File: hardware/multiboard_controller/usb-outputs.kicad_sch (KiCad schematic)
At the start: 24 parts, among them J2 USB_C_Receptacle, J3 USB_C_Receptacle, J4 USB_C_Receptacle, J5 USB_C_Receptacle, J6 USB_C_Receptacle, J7 USB_C_Receptacle, J8 USB_C_Receptacle, J9 USB_C_Receptacle

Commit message: Adding final connectors and general cleanup.
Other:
- note added: "Nopo all but 2 for validation"
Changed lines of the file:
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@@
+		)
+	)
+	(text "Nopo all but 2 for validation\n"
+		(exclude_from_sim no)
+		(at 138.938 24.384 0)
+		(effects
+			(font
+				(size 1.27 1.27)
+			)
 		)
 	)

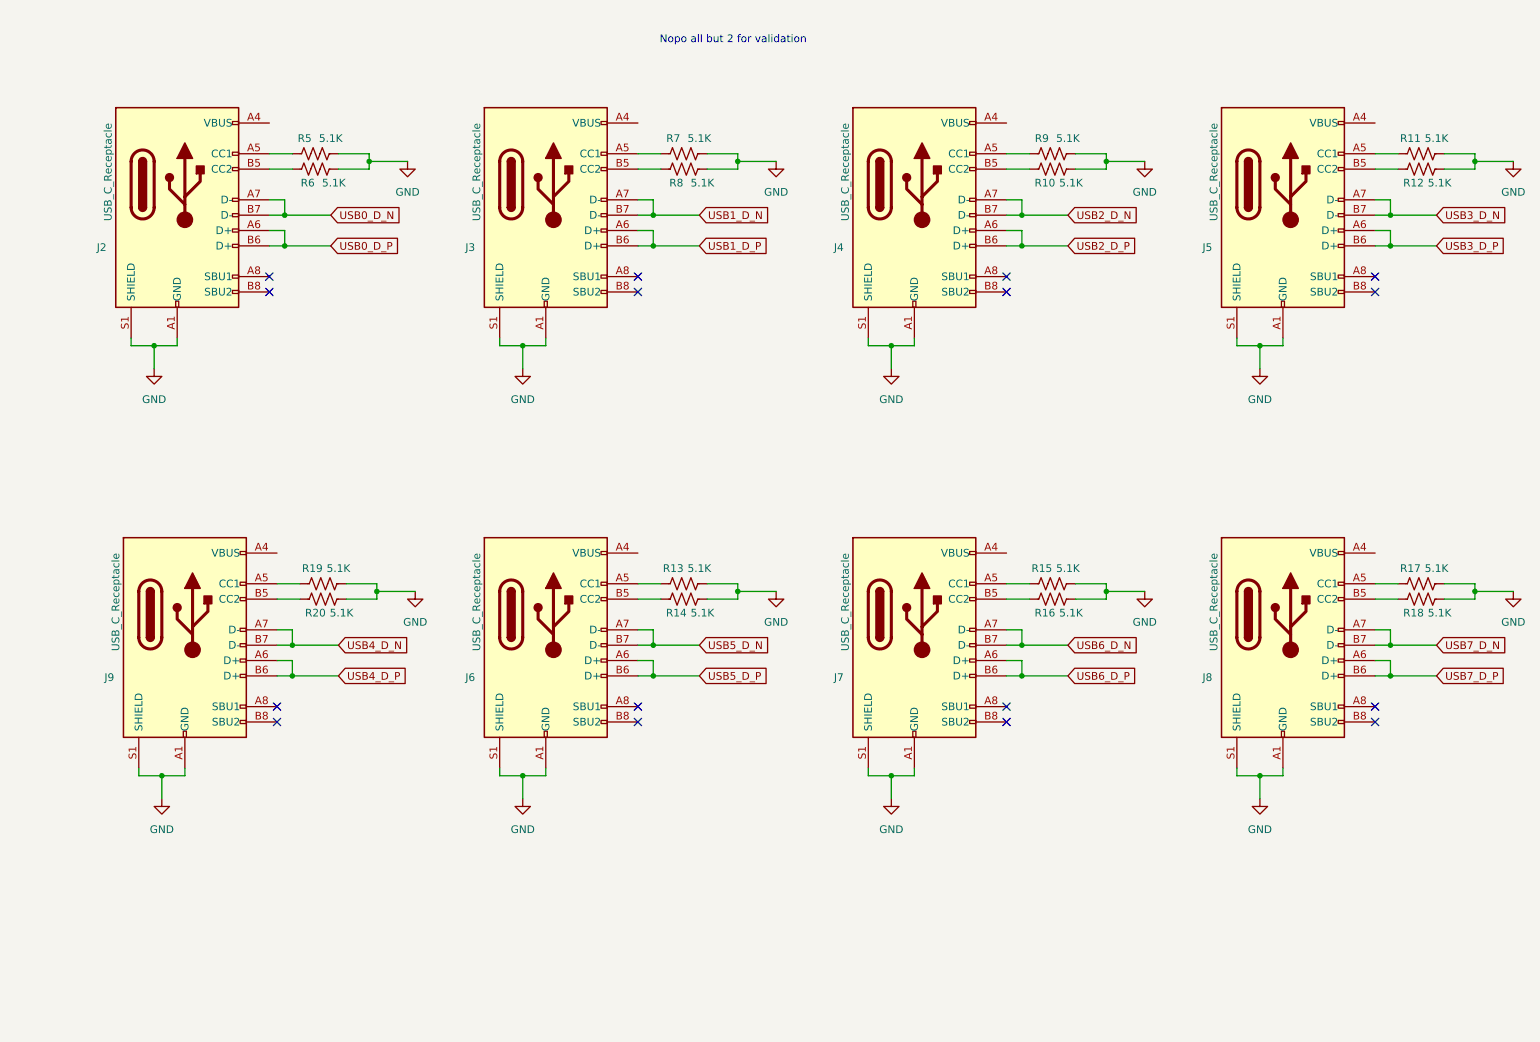
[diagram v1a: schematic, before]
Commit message: Starting layout
Add serial ground connections, add footprint libraries, start layout.
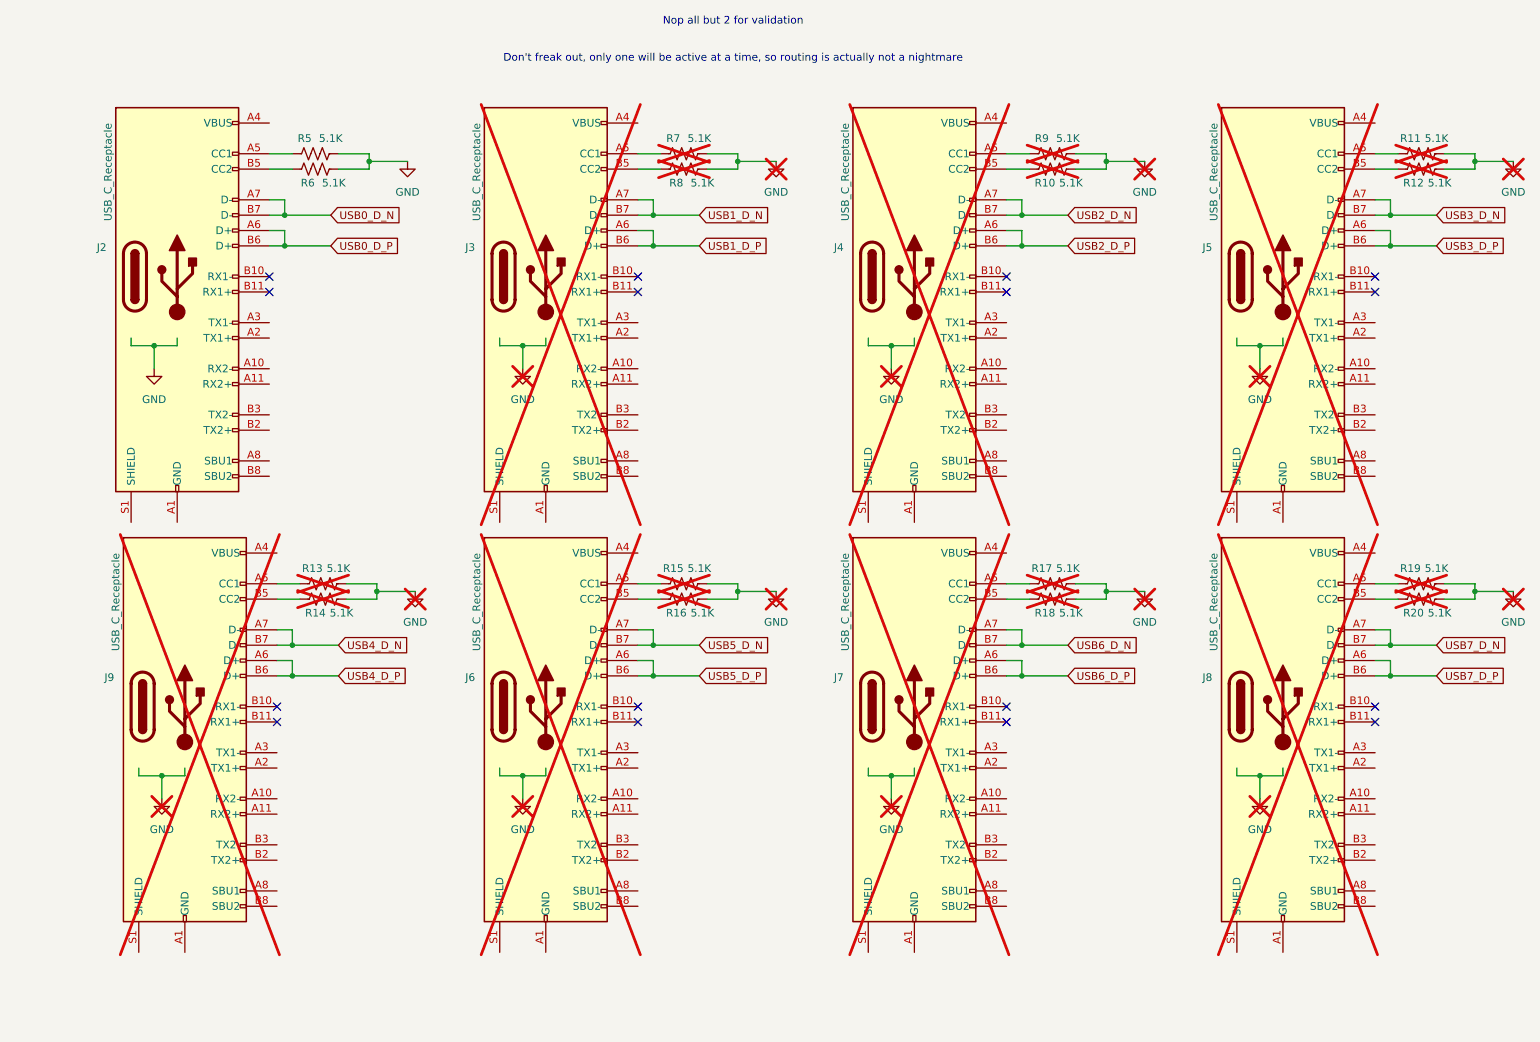
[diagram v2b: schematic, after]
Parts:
- J2: footprint (none) -> Connector_USB:USB_C_Receptacle_GCT_USB4135-GF-A_6P_TopMnt_Horizontal
- J3, J4, J5, J6, J7, J8, J9: footprint (none) -> Connector_USB:USB_C_Receptacle_GCT_USB4135-GF-A_6P_TopMnt_Horizontal; now not fitted
- R10, R11, R12, R13, R14, R15, R16, R17, R18, R19, R20, R7, R8, R9: footprint (none) -> Resistor_SMD:R_0402_1005Metric; now not fitted
- R5, R6: footprint (none) -> Resistor_SMD:R_0402_1005Metric
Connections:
- net GND: no longer J2.A1 (GND), J2.A12 (GND), J2.B1 (GND), J2.B12 (GND), J2.S1 (SHIELD), J3.A1 (GND), J3.A12 (GND), J3.B1 (GND), J3.B12 (GND), J3.S1 (SHIELD), J4.A1 (GND), J4.A12 (GND), J4.B1 (GND), J4.B12 (GND), J4.S1 (SHIELD), J5.A1 (GND), J5.A12 (GND), J5.B1 (GND), J5.B12 (GND), J5.S1 (SHIELD), J6.A1 (GND), J6.A12 (GND), J6.B1 (GND), J6.B12 (GND), J6.S1 (SHIELD), J7.A1 (GND), J7.A12 (GND), J7.B1 (GND), J7.B12 (GND), J7.S1 (SHIELD), J8.A1 (GND), J8.A12 (GND), J8.B1 (GND), J8.B12 (GND), J8.S1 (SHIELD), J9.A1 (GND), J9.A12 (GND), J9.B1 (GND), J9.B12 (GND), J9.S1 (SHIELD)
- net at J6.A5 (CC1): now also R15.1; no longer R13.1
- net at J6.B5 (CC2): now also R16.1; no longer R14.1
- net at J9.B5 (CC2): now also R14.1; no longer R20.1
- net at R19.1: now also J8.A5 (CC1); no longer J9.A5 (CC1)
- net at R17.1: now also J7.A5 (CC1); no longer J8.A5 (CC1)
- net at J8.B5 (CC2): now also R20.1; no longer R18.1
- net at J7.B5 (CC2): now also R18.1; no longer R16.1
- new net: J6.A1 (GND), J6.A12 (GND), J6.B1 (GND), J6.B12 (GND)
- new net: J2.A1 (GND), J2.A12 (GND), J2.B1 (GND), J2.B12 (GND)
- new net: J4.A1 (GND), J4.A12 (GND), J4.B1 (GND), J4.B12 (GND)
- new net: J8.A1 (GND), J8.A12 (GND), J8.B1 (GND), J8.B12 (GND)
- new net: J9.A1 (GND), J9.A12 (GND), J9.B1 (GND), J9.B12 (GND)
- new net: J9.A5 (CC1), R13.1
- new net: J5.A1 (GND), J5.A12 (GND), J5.B1 (GND), J5.B12 (GND)
- new net: J3.A1 (GND), J3.A12 (GND), J3.B1 (GND), J3.B12 (GND)
- new net: J7.A1 (GND), J7.A12 (GND), J7.B1 (GND), J7.B12 (GND)
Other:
- note added: "Nop all but 2 for validation Don't freak out, only one will be active at a time, so routing is actually not a nightmare"
- note removed: "Nopo all but 2 for validation"

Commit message: Updating connections to USB output connectors, prepped subsystems for board layout.
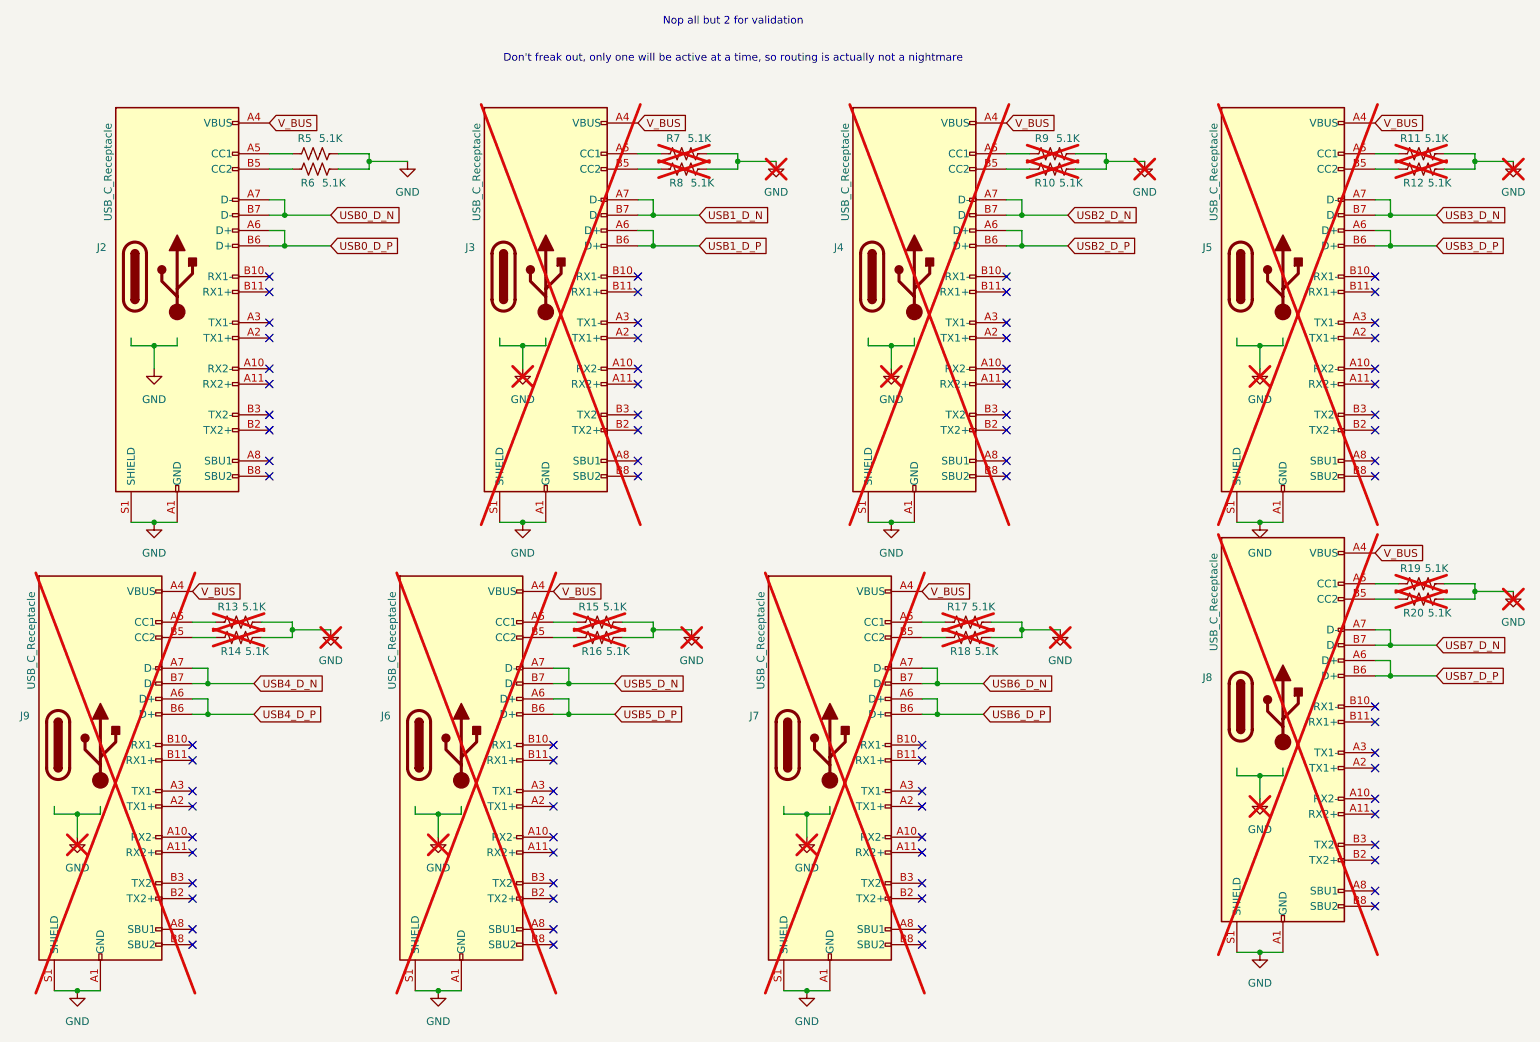
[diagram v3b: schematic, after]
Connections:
- net GND: now also J2.A1 (GND), J2.A12 (GND), J2.B1 (GND), J2.B12 (GND), J2.S1 (SHIELD), J3.A1 (GND), J3.A12 (GND), J3.B1 (GND), J3.B12 (GND), J3.S1 (SHIELD), J4.A1 (GND), J4.A12 (GND), J4.B1 (GND), J4.B12 (GND), J4.S1 (SHIELD), J5.A1 (GND), J5.A12 (GND), J5.B1 (GND), J5.B12 (GND), J5.S1 (SHIELD), J6.A1 (GND), J6.A12 (GND), J6.B1 (GND), J6.B12 (GND), J6.S1 (SHIELD), J7.A1 (GND), J7.A12 (GND), J7.B1 (GND), J7.B12 (GND), J7.S1 (SHIELD), J8.A1 (GND), J8.A12 (GND), J8.B1 (GND), J8.B12 (GND), J8.S1 (SHIELD), J9.A1 (GND), J9.A12 (GND), J9.B1 (GND), J9.B12 (GND), J9.S1 (SHIELD)
- net V_BUS: now reaches J6.A4 (VBUS), J6.A9 (VBUS), J6.B4 (VBUS), J6.B9 (VBUS)
- net V_BUS: now also J2.A4 (VBUS), J2.A9 (VBUS), J2.B4 (VBUS), J2.B9 (VBUS), J3.A4 (VBUS), J3.A9 (VBUS), J3.B4 (VBUS), J3.B9 (VBUS), J4.A4 (VBUS), J4.A9 (VBUS), J4.B4 (VBUS), J4.B9 (VBUS), J5.A4 (VBUS), J5.A9 (VBUS), J5.B4 (VBUS), J5.B9 (VBUS), J7.A4 (VBUS), J7.A9 (VBUS), J7.B4 (VBUS), J7.B9 (VBUS), J8.A4 (VBUS), J8.A9 (VBUS), J8.B4 (VBUS), J8.B9 (VBUS), J9.A4 (VBUS), J9.A9 (VBUS), J9.B4 (VBUS), J9.B9 (VBUS)
- no-connect marks 16 -> 80
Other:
- moved on the sheet: J6, J7, J9, R13, R14, R15, R16, R17, R18
